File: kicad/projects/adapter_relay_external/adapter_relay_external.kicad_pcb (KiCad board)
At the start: 2 copper layers, 50 x 50 mm, 20 parts, among them J1 M5Stack A117 PinHeader, J2 M5Stack A117 PinSocket, J3 DC-0440-2.5A-2.0, U1 Optocoupler

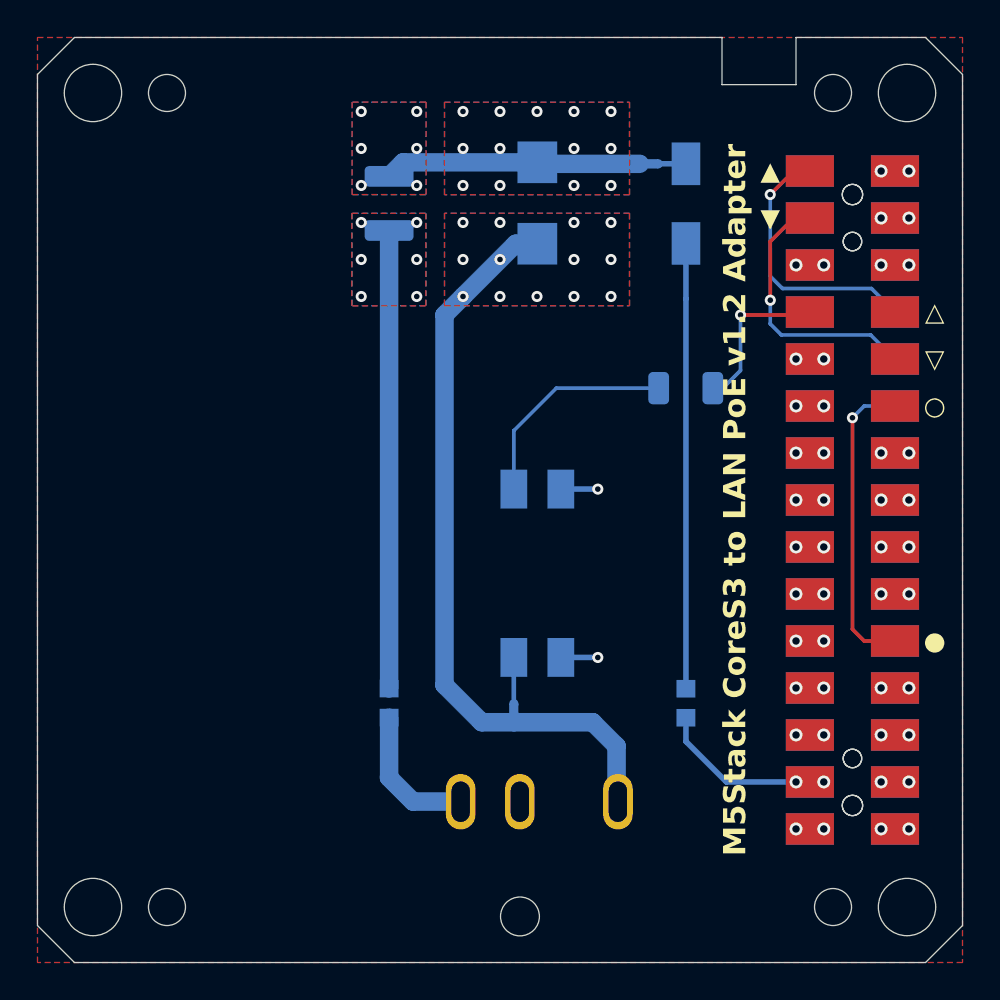
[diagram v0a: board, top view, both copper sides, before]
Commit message: tune dc jack footprint and pcb placement
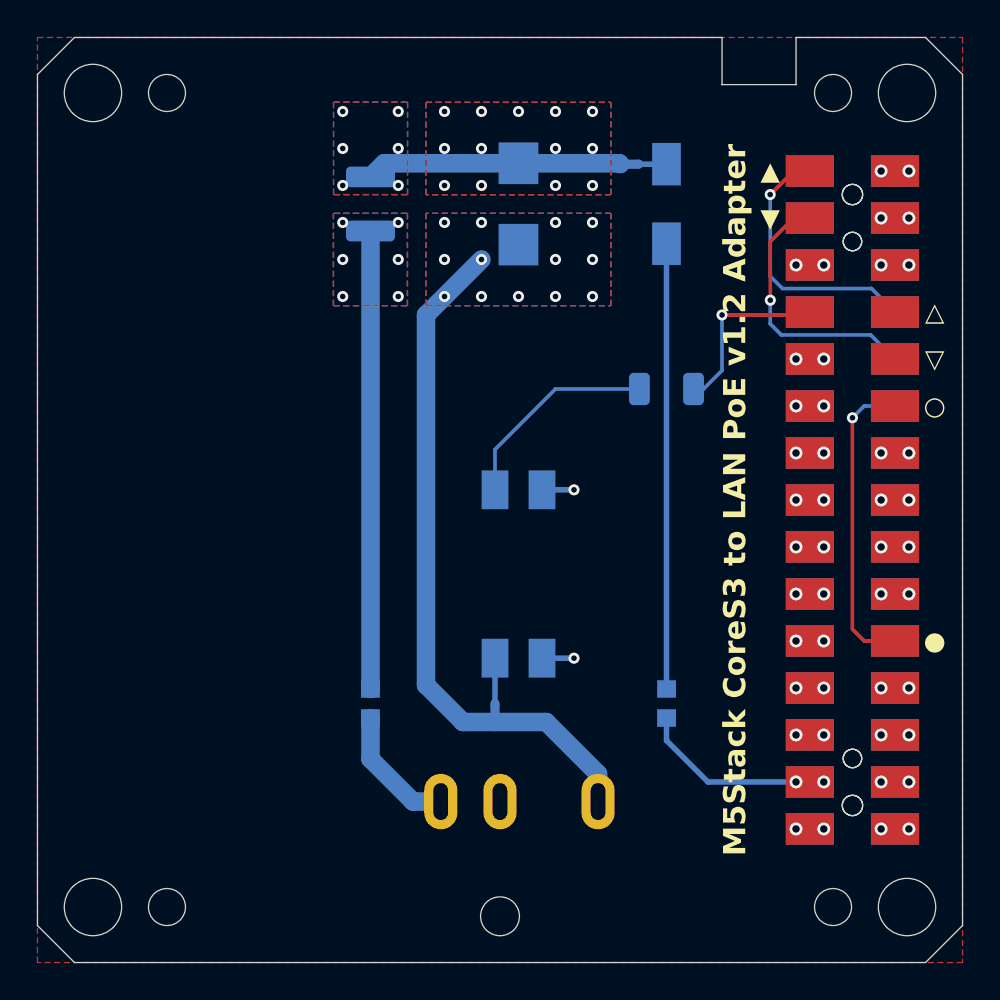
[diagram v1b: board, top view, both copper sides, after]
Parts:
- moved J3 1.07 mm to (125.0, 147.5)
- moved D1 1.05 mm to (134.0, 109.0)
- moved NT1 1.05 mm to (132.0, 106.8)
- moved F1 1.05 mm to (134.0, 136.0)
- moved R2 1.04 mm to (134.0, 119.0)
- moved D2 1.02 mm to (126.0, 109.0)
- moved U1 1.02 mm to (126.0, 129.0)
- moved NT2 1.02 mm to (124.7, 136.5)
- moved R1 1.01 mm to (118.0, 109.0)
- moved F2 1.01 mm to (118.0, 136.0)
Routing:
- net /-LOAD: track 40.3 -> 37.0 mm
- net +5V: track 8.14 -> 9.89 mm
- net /G5·: track 8.75 -> 9.77 mm
- net /+LOAD: track 7.58 -> 6.97 mm
- net /LED: track 11.9 -> 11.3 mm
- net GND: track 4.00 -> 3.46 mm

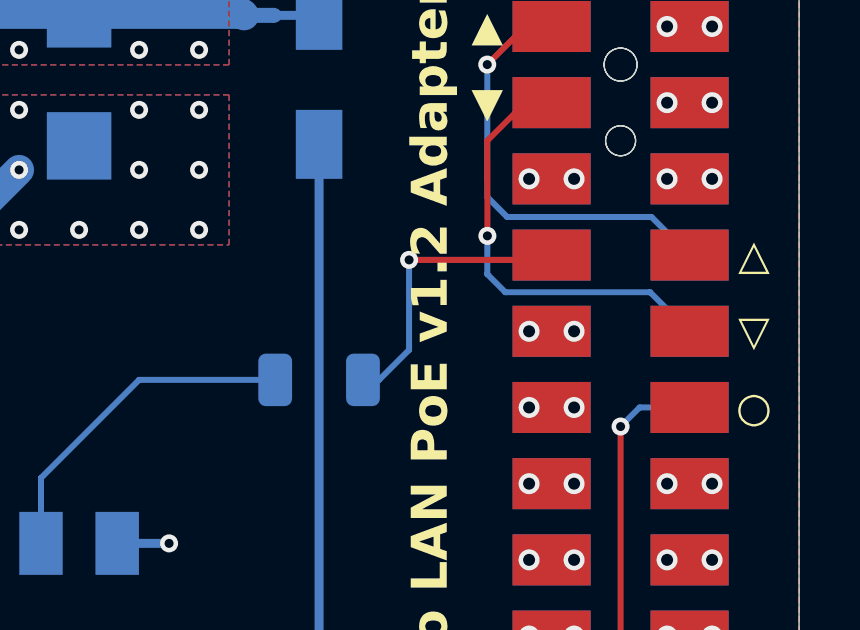
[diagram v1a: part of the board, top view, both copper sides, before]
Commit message: move dc jack, tune R1 spec, add gpio pin
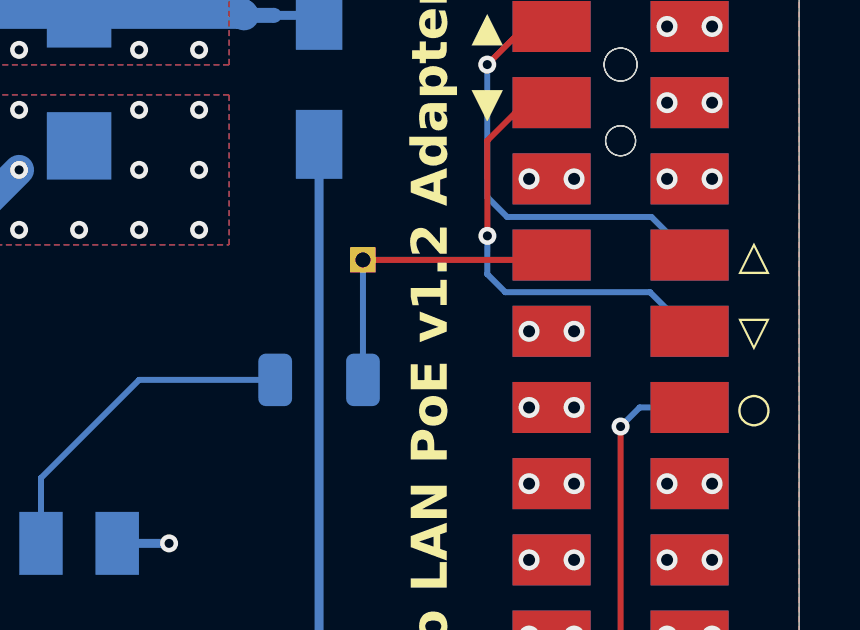
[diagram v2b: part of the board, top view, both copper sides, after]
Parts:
- added J4: Conn_01x01_Pin, Connector_PinHeader_1.00mm:PinHeader_1x01_P1.00mm_Vertical, B.Cu at (135.5, 115.0)
- F1: value 10/50mA -> 10/50mA 15/100Ω
- F2: value 80/200mA -> 80/200mA 2.5/12Ω
- R1: value 82 -> 33 1W
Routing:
- net /G5·: track 9.77 -> 10.4 mm, vias 1 -> 0
